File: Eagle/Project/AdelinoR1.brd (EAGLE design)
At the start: 47 x 53.3 mm, 67 parts, among them J1 DC-044-A, J2 YELLOW-8P-2.54, J3 YELLOW-6P-2.54, J4 YELLOW-8P-2.54, J5 YELLOW-8P-2.54, J6 4P-2.0, J7 YELLOW-2X3P-2.54, J8 4P-2.0, Q1 NCE3407A, Q2 CJ2305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

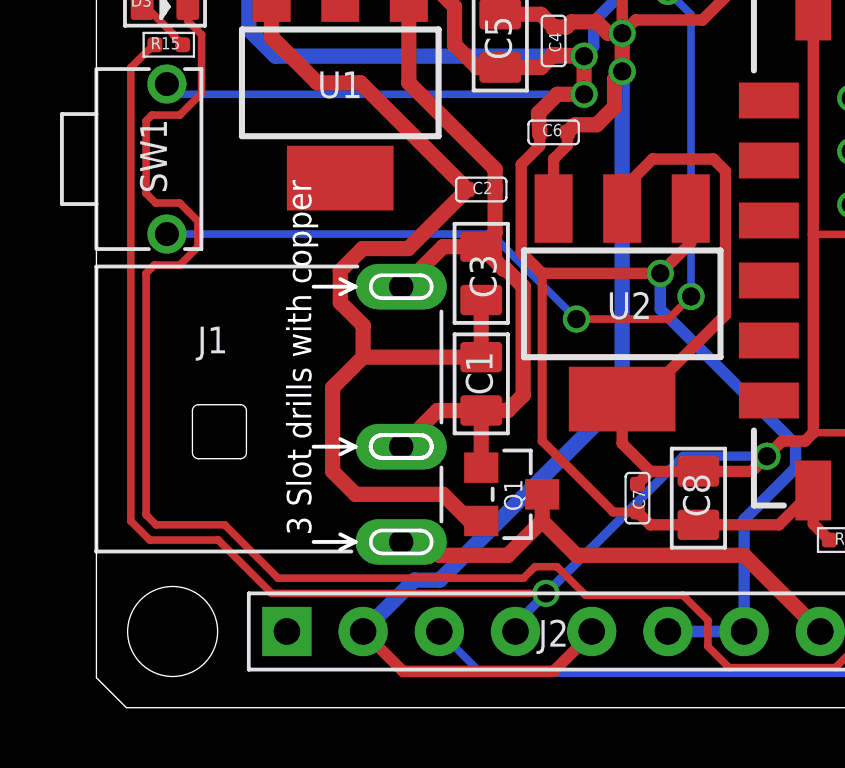
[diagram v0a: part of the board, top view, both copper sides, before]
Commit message: Fix J1 DC-044 pin drilling; fix J7 dip male header 2X3P pin diameter.
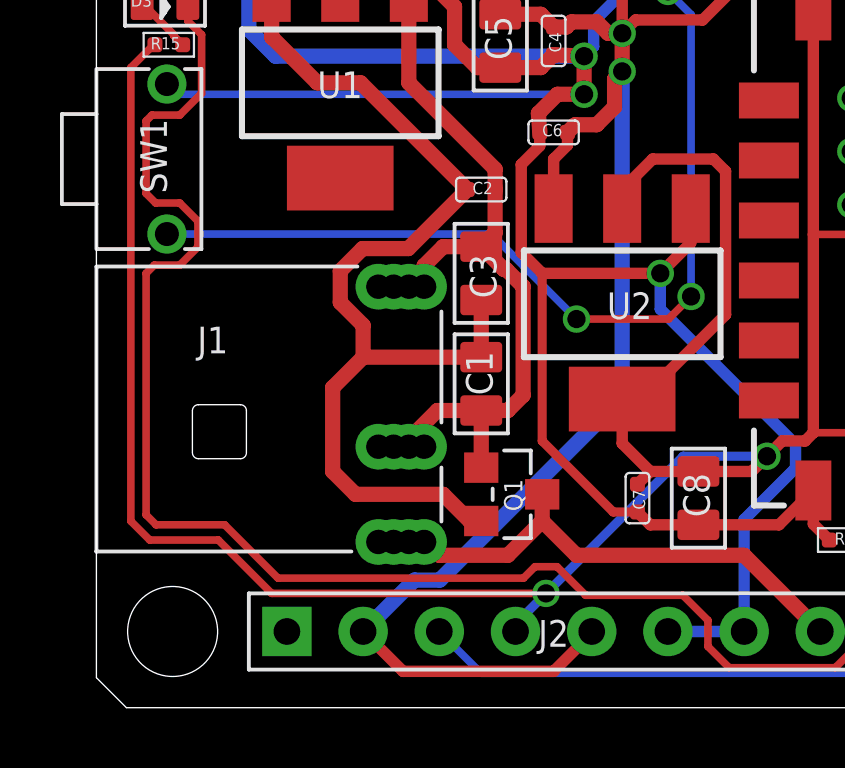
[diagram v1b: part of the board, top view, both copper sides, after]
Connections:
- net GND: now also J1.CDN1, J1.CDN2, J1.CDN3, J1.CDN4, J1.GND1, J1.GND2, J1.GND3, J1.GND4; no longer J1.-, J1.CDN
- net VIN: now also J1.VCC1, J1.VCC2, J1.VCC3, J1.VCC4; no longer J1.+
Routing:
- net GND: track 292.8 -> 296.4 mm
- net VIN: track 17.0 -> 18.3 mm
